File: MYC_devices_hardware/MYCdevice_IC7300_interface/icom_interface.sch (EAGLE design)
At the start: 42 parts, among them IC1 ATMEGA1284, IC2 MAX232, IC3 PCA9517, IC4 78L05, Q1 20MHz, Q2 BC817-40SMD, Q3 BC817-40SMD, Q4 BSS138, X1 8-15V, X2 1503_09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

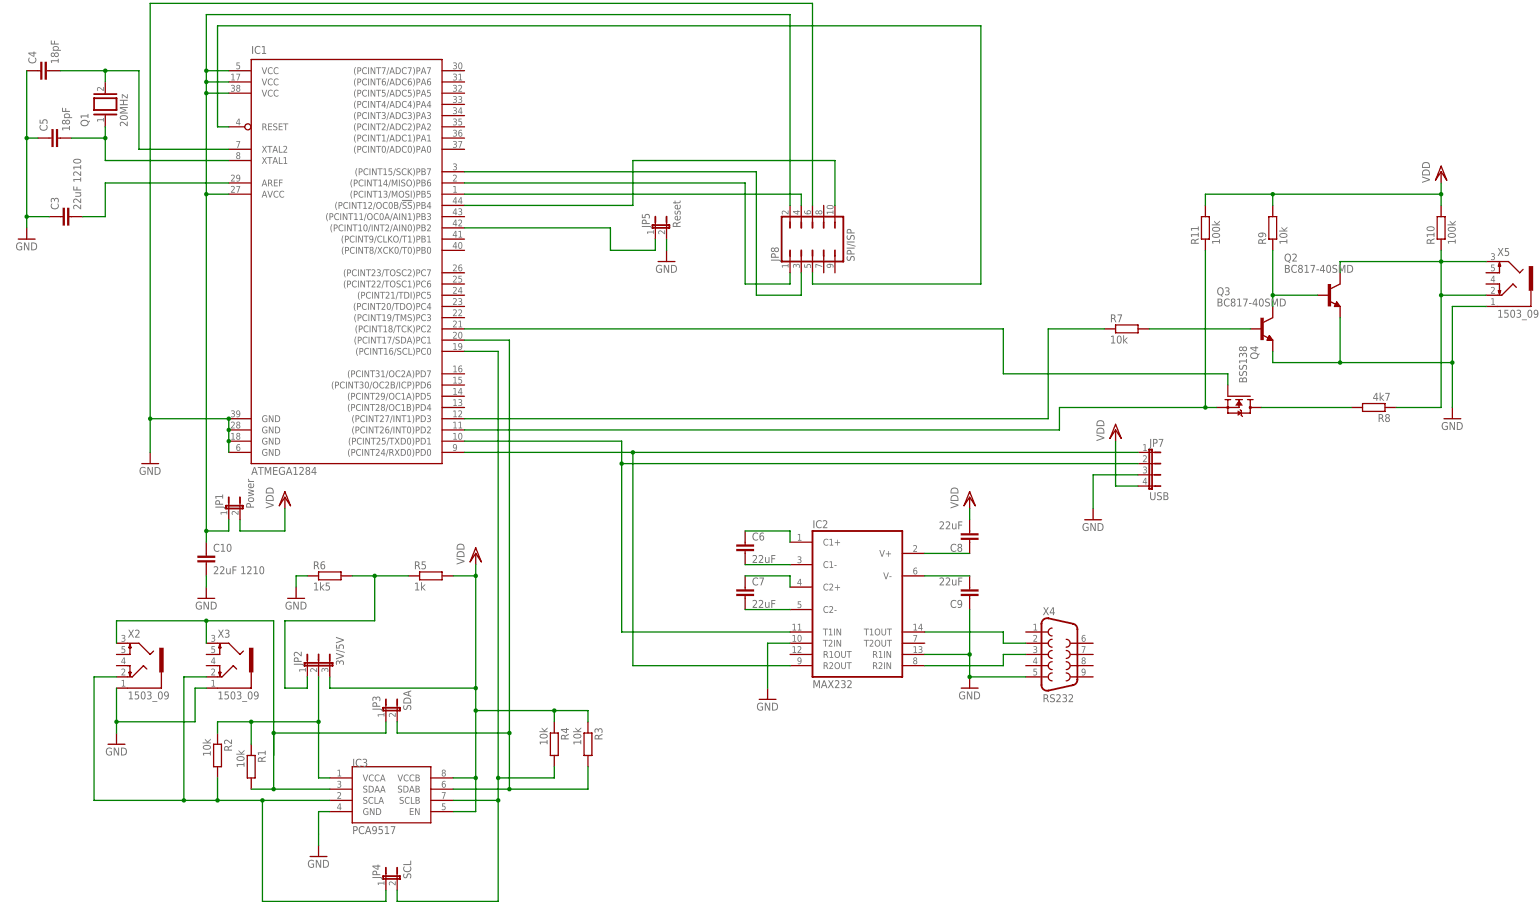
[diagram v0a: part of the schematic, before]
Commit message: wrong FET corrected, better layout
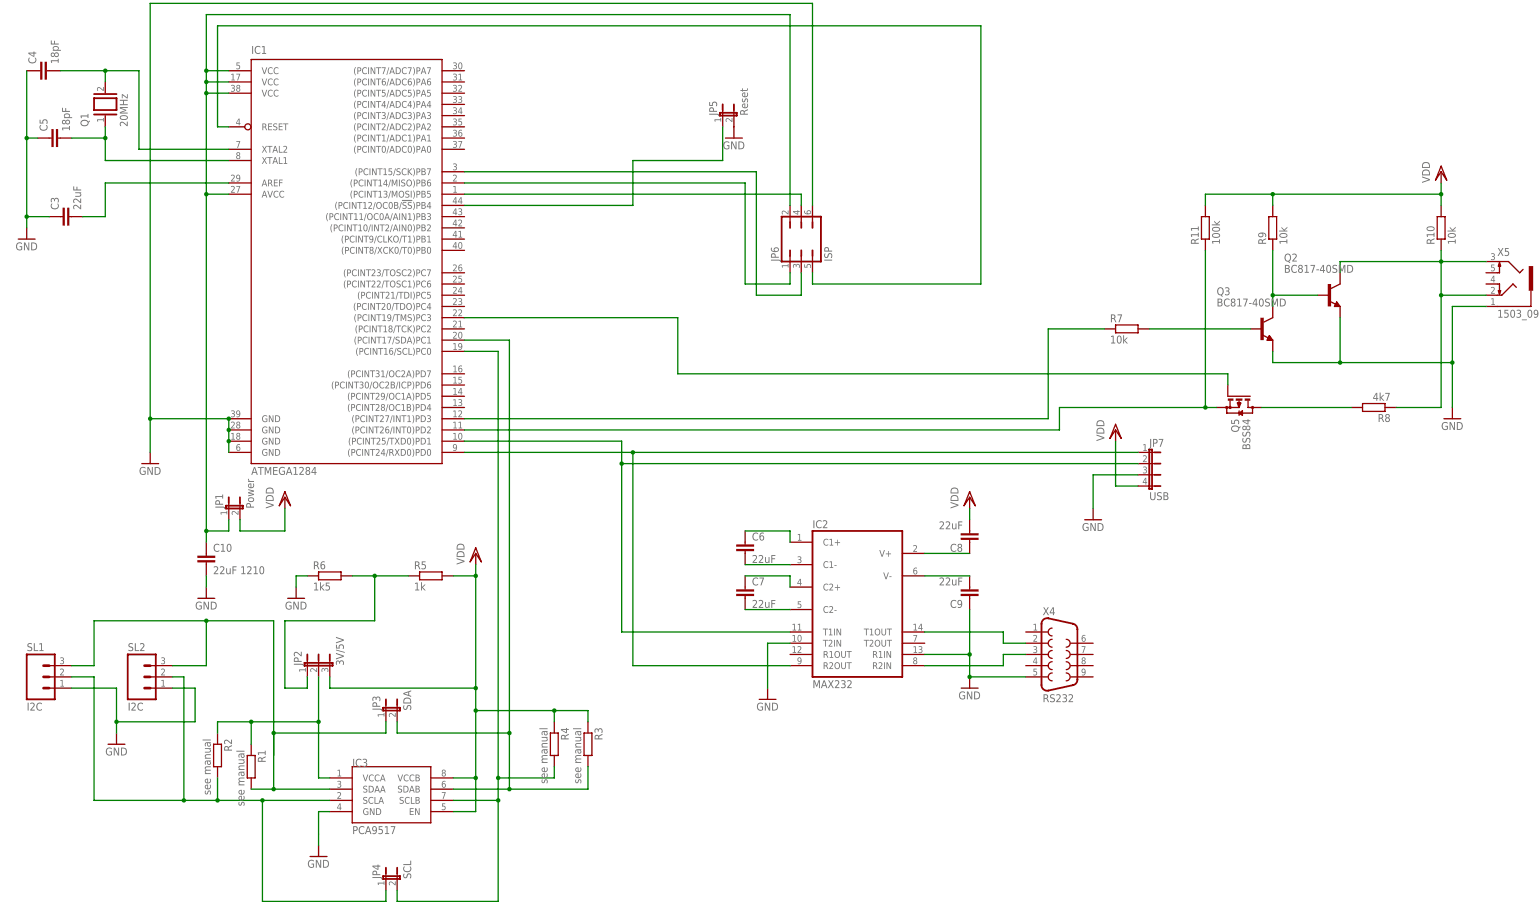
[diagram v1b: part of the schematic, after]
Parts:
- removed JP8: SPI/ISP, jumper:JP5Q
- removed Q4: BSS138, bss138_10:BSS138
- removed X2, X3: 1503_09, con-lumberg:1503_09
- added JP6: ISP, jumper:JP3Q
- added Q5: BSS84, transistor-small-signal:BSS84
- added SL1, SL2: I2C, con-amp-quick:M03
- C3: value 22uF 1210 -> 22uF
- R1, R2, R3, R4: value 10k -> see manual
- R10: value 100k -> 10k
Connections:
- removed net N$4: IC1.(PCINT10/INT2/AIN0)PB2, JP5.1
- net GND: now also JP6.6, SL1.1, SL2.1; no longer JP8.6, X2.1, X3.1
- net N$15: now also JP5.1; no longer JP8.10
- net N$18: now also JP6.5; no longer JP8.5
- net N$19: now also Q5.S; no longer Q4.S
- net N$20: now also JP6.3; no longer JP8.3
- net N$23: now also SL1.3, SL2.3; no longer X2.3, X3.3
- net N$25: now also SL1.2, SL2.2; no longer X2.2, X3.2
- net N$28: now also JP6.4; no longer JP8.4
- net N$29: now also Q5.D; no longer Q4.D
- net N$34: now also IC1.(PCINT19/TMS)PC3, Q5.G; no longer IC1.(PCINT18/TCK)PC2, Q4.G
- net N$6: now also JP6.1; no longer JP8.1
- net N$7: now also JP6.2; no longer JP8.2
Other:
- moved on the sheet: JP5

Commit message: bascom added, and new board
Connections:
- net N$15: now also IC1.(PCINT10/INT2/AIN0)PB2; no longer IC1.(PCINT12/OC0B/!SS!)PB4
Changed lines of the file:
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@@
 <net name="N$15" class="0">
 <segment>
-<pinref part="IC1" gate="G$1" pin="(PCINT12/OC0B/!SS!)PB4"/>
-<wire x1="111.76" y1="271.78" x2="149.86" y2="271.78" width="0.1524" layer="91"/>
-<wire x1="149.86" y1="271.78" x2="149.86" y2="281.94" width="0.1524" layer="91"/>
+<wire x1="149.86" y1="266.7" x2="149.86" y2="281.94" width="0.1524" layer="91"/>
 <wire x1="149.86" y1="281.94" x2="170.18" y2="281.94" width="0.1524" layer="91"/>
 <pinref part="JP5" gate="A" pin="1"/>
 <wire x1="170.18" y1="289.56" x2="170.18" y2="281.94" width="0.1524" layer="91"/>
+<pinref part="IC1" gate="G$1" pin="(PCINT10/INT2/AIN0)PB2"/>
+<wire x1="111.76" y1="266.7" x2="149.86" y2="266.7" width="0.1524" layer="91"/>
 </segment>
 </net>
